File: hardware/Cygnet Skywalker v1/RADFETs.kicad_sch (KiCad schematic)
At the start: 18 parts, among them Q2 NJFET, Q3 NJFET, Q4 NMOS, Q5 NMOS, U11 RM-VT01-A Readout Module, U17 LM234Z-6, U6 VT01

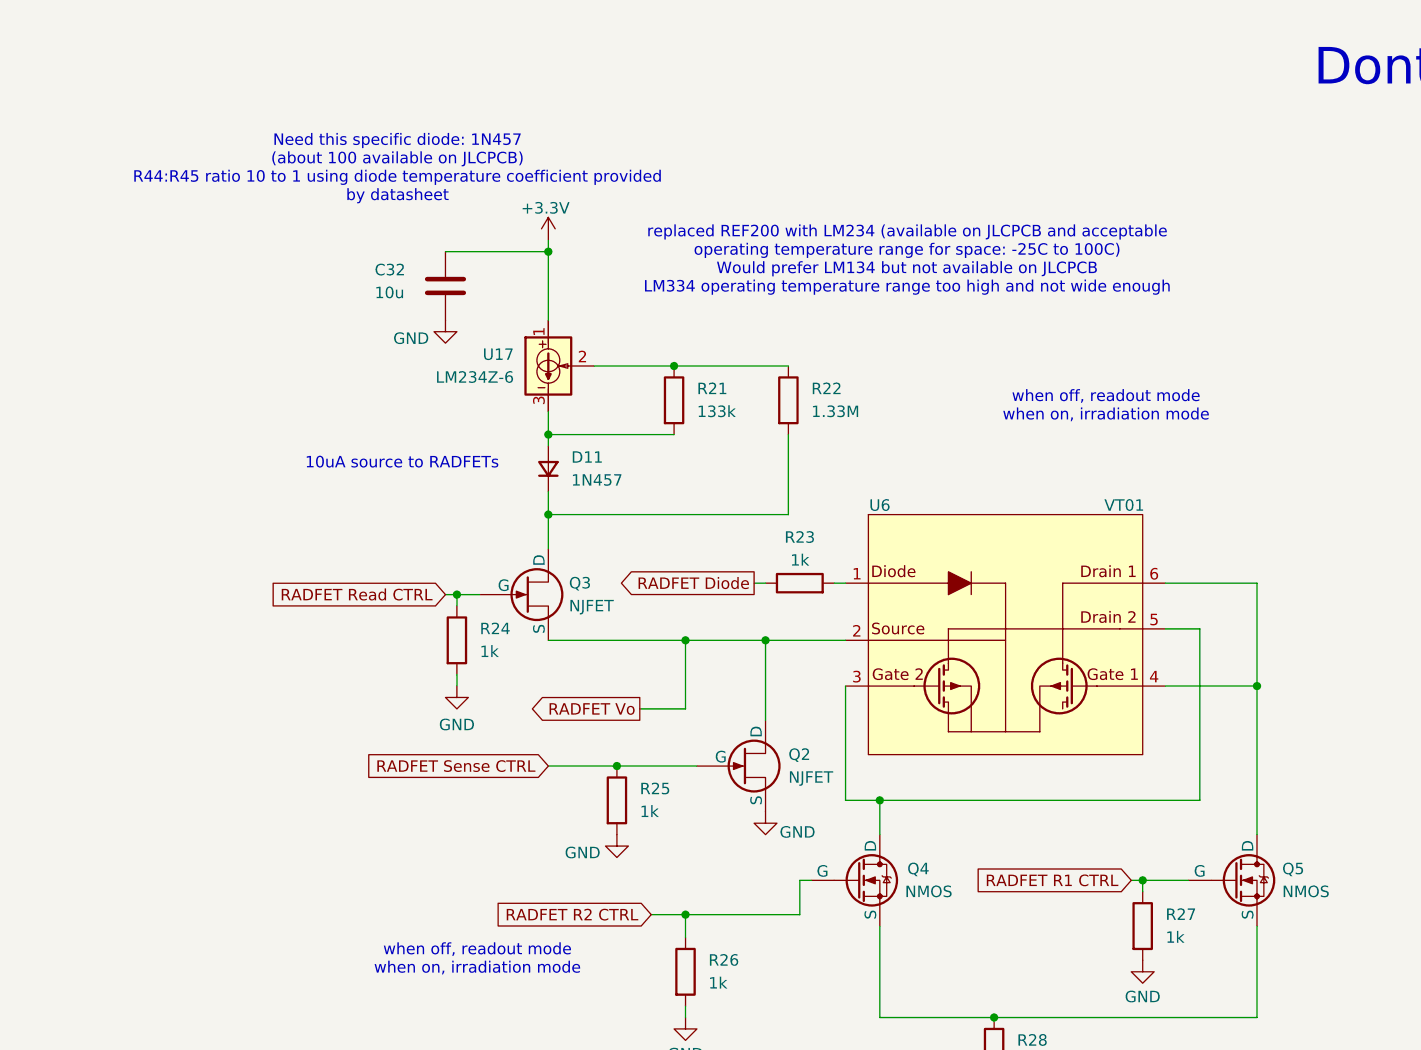
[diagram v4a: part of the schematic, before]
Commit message: updated schematic with mosfets
jfets no more for now. Also added footprints to some symbols.
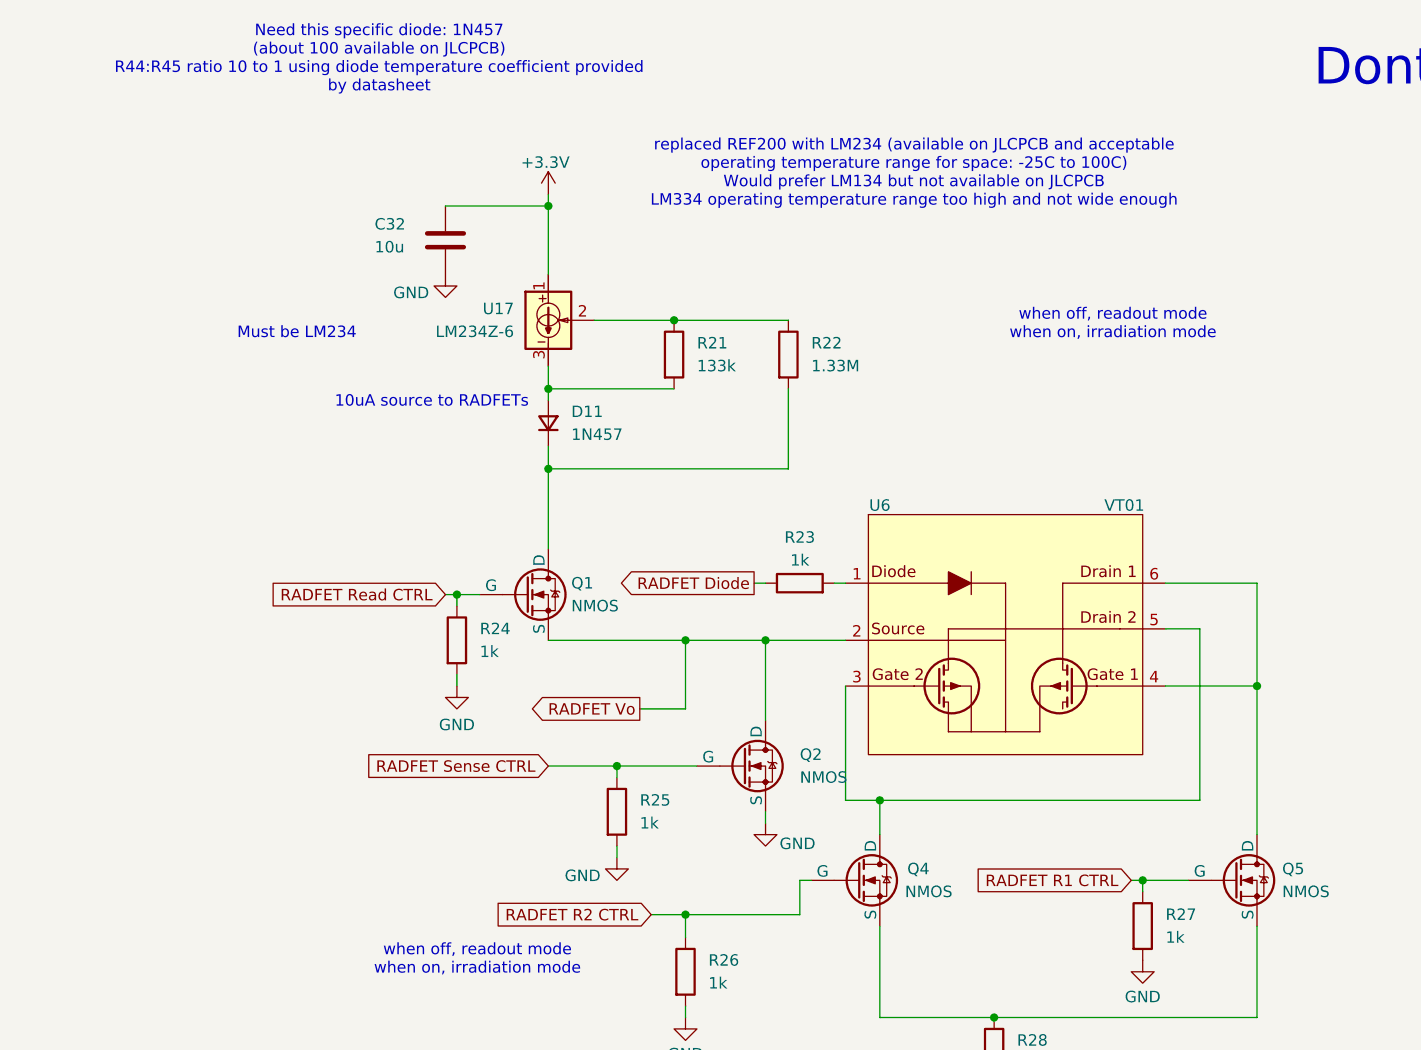
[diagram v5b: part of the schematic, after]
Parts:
- removed Q2, Q3: NJFET, symbol Simulation_SPICE:NJFET
- added Q1, Q2: NMOS, symbol Simulation_SPICE:NMOS
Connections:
- net GND: now also Q2.3 (S)
- net RADFET Read CTRL: now also Q1.2 (G)
- net RADFET Sense CTRL: now also Q2.2 (G)
- net RADFET Vo: now also Q1.3 (S), Q2.1 (D)
- net at D11.1 (K), R22.2: now also Q1.1 (D)
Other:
- note added: "Must be LM234"
- moved on the sheet: C32, D11, R21, R22, R25, U17

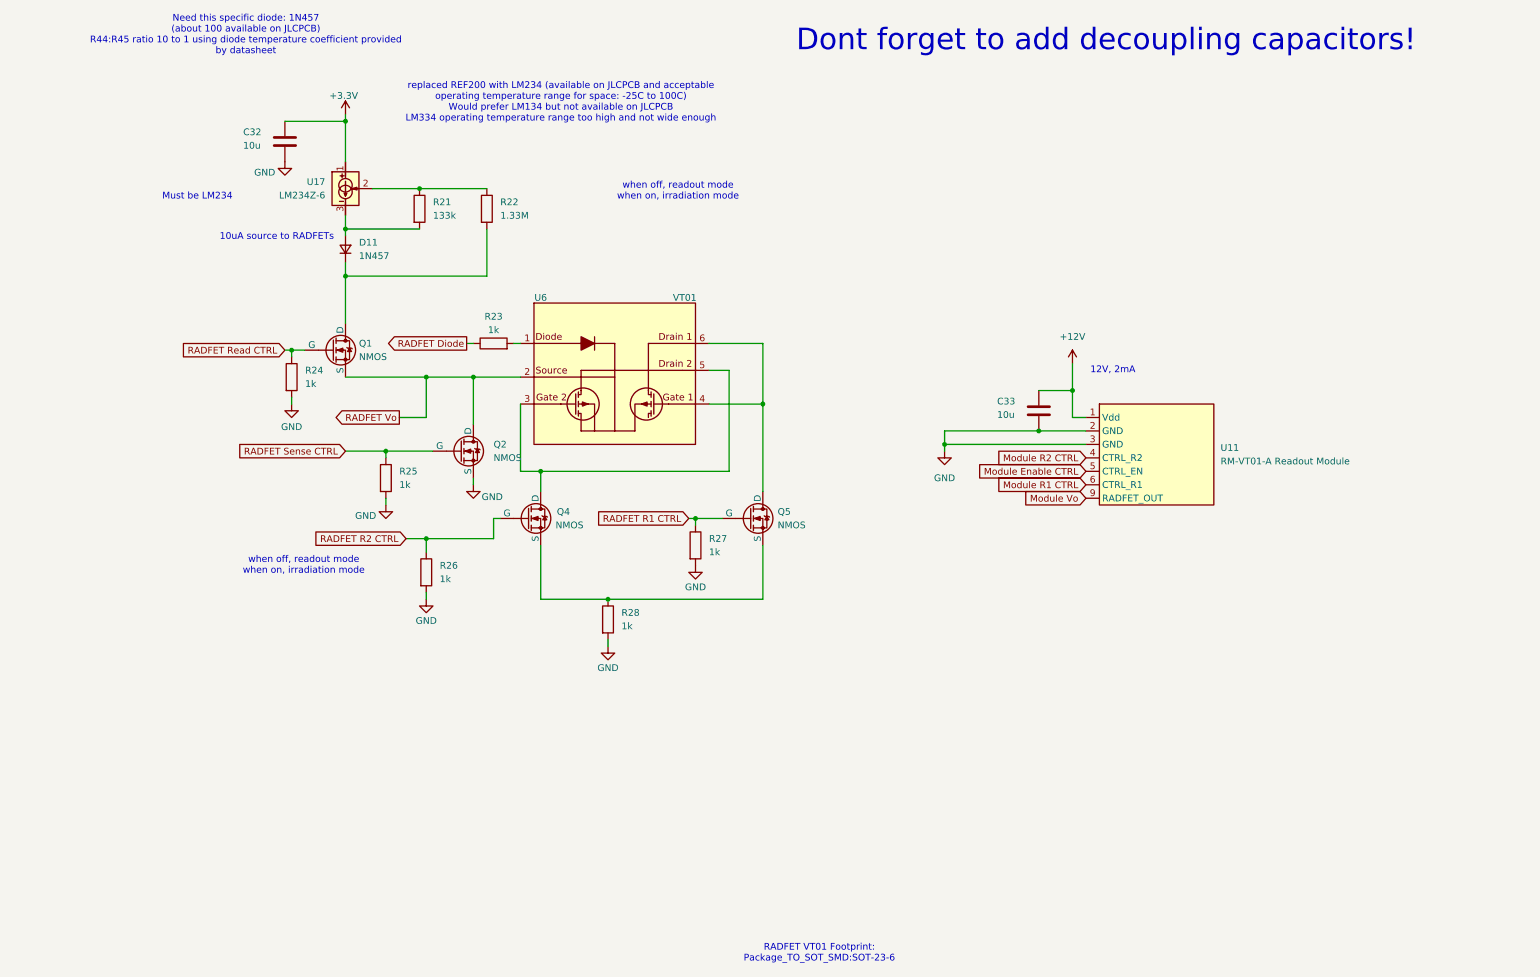
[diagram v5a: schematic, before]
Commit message: changes to radfet readout design
- using analog switch ic to switch between sense & readout (tmux1133)
- added non inverting buffer for voltage readout
- haven't fully deep dived into the new components & must look into more
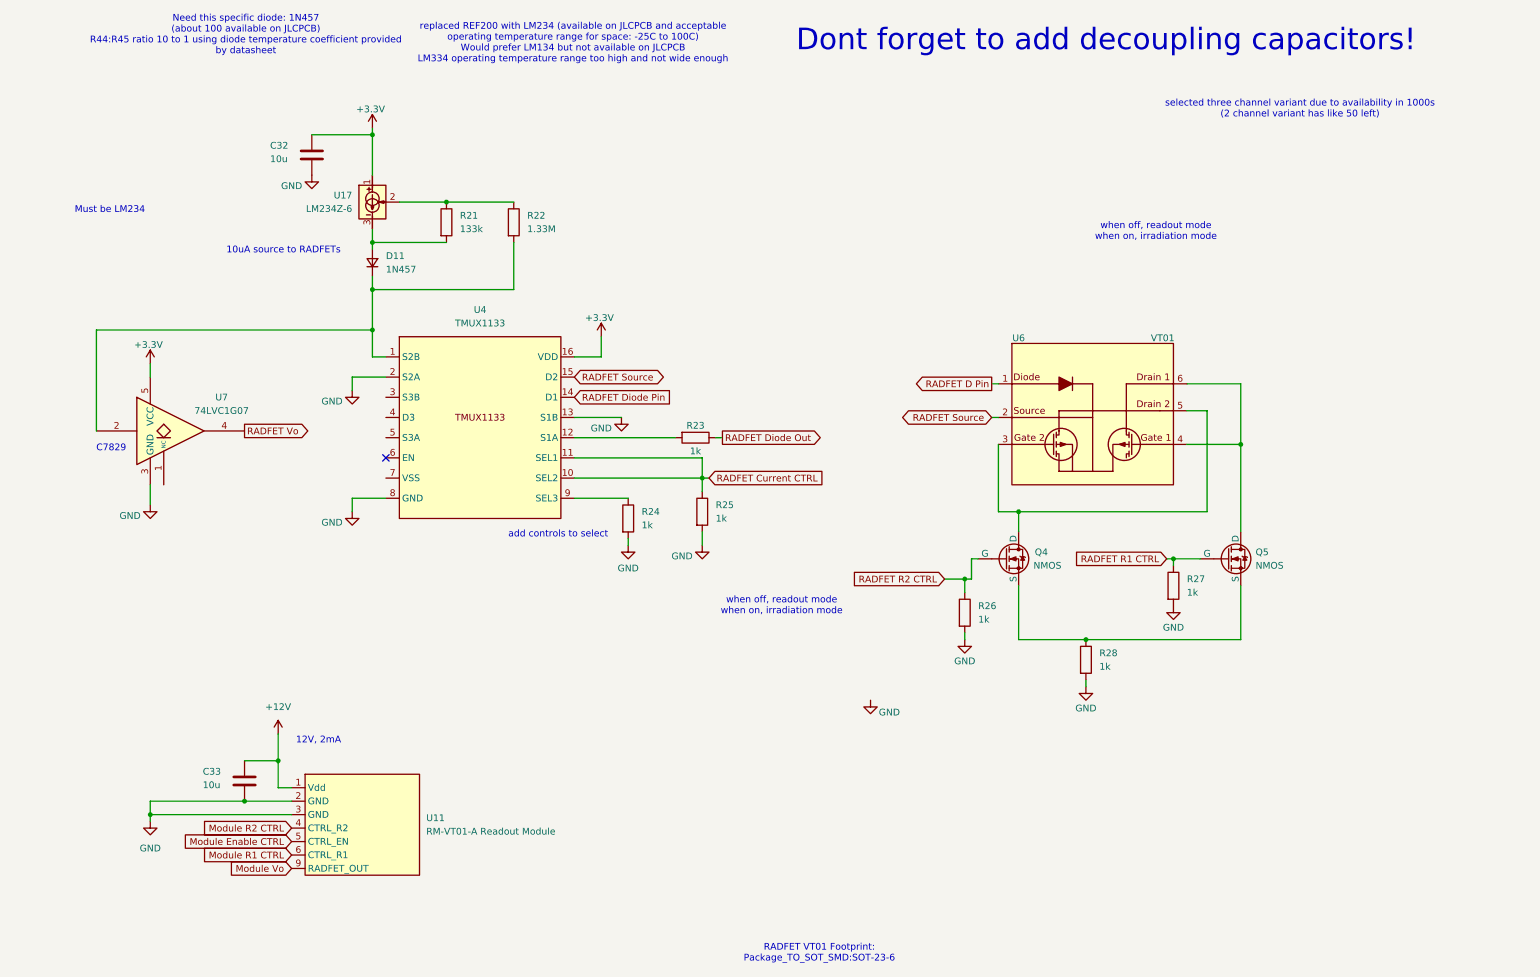
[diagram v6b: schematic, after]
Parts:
- removed Q1, Q2: NMOS, symbol Simulation_SPICE:NMOS
- added U4: TMUX1133, symbol Cygnet Skywalker v1:TMUX1133
- added U7: 74LVC1G07, Package_TO_SOT_SMD:SOT-23-5, symbol 74xGxx:74LVC1G07
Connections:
- net +3.3V: now also U4.16 (VDD), U7.5 (VCC)
- net GND: now also U4.13 (S1B), U4.2 (S2A), U4.8 (GND), U7.3 (GND)
- net RADFET Vo: now also U7.4; no longer U6.2
- net at R23.2: now also U4.12 (S1A); no longer U6.1
- net at D11.1 (K), R22.2: now also U4.1 (S2B), U7.2
- net RADFET Diode renamed RADFET Diode Out
- net RADFET Read CTRL: no longer names the net of R24.1
- net RADFET Read CTRL: now also U4.9 (SEL3)
- net RADFET Sense CTRL renamed RADFET Current CTRL
- net RADFET Current CTRL: now also U4.10 (SEL2), U4.11 (SEL1)
- new net RADFET D Pin: U6.1
- new net RADFET Diode Pin: U4.14 (D1)
- new net RADFET Source: U4.15 (D2), U6.2
- no-connect marks 0 -> 1
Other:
- note added: "C7829"
- note added: "add controls to select"
- note added: "selected three channel variant due to availability in 1000s (2 channel variant has like 50 left)"
- moved on the sheet: C32, C33, D11, Q4, Q5, R21, R22, R23, R24, R25, R26, R27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

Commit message: added op amp
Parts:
- added U15: OPA4H199-SEP, symbol Cygnet Skywalker v1:OPA4H199-SEP
- U4: footprint (none) -> Package_SO:TSSOP-16_4.4x5mm_P0.65mm
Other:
- note added: "OP AMP with +-10nA current leakage max"
- note added: "just found out leakage current is around +-5uA :skull:"
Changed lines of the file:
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@@
 	(generator_version "9.0")
 	(paper "A4")
+	(text "just found out leakage current is around +-5uA :skull:"
+		(exclude_from_sim no)
+		(at 38.354 106.426 0)
+		(effects
+			(font
+				(size 1.27 1.27)
+			)
+		)
+	)
 	(text "add controls to select"
 		(exclude_from_sim no)
@@
 		)
 	)
+	(text "OP AMP with +-10nA current leakage max"
+		(exclude_from_sim no)
+		(at 118.364 127.254 0)
+		(effects
+			(font
+				(size 1.27 1.27)
+			)
+		)
+	)
 	(text "Dont forget to add decoupling capacitors!"
 		(exclude_from_sim no)
@@
 	(text "when off, readout mode\nwhen on, irradiation mode"
 		(exclude_from_sim no)
-		(at 150.876 128.27 0)
+		(at 245.872 156.21 0)
 		(effects
 			(font
@@
 	)
 	(symbol
+		(lib_id "Cygnet Skywalker v1:OPA4H199-SEP")
+		(at 139.7 134.62 0)
+		(unit 1)
+		(exclude_from_sim no)
+		(in_bom yes)
+		(on_board yes)
+		(dnp no)
+		(fields_autoplaced yes)
+		(property "Reference" "U15"
+			(at 139.7 129.54 0)
+			(effects
+				(font
+					(size 1.27 1.27)
+				)
+			)
+		)
+		(property "Value" "OPA4H199-SEP"
+			(at 139.7 132.08 0)
+			(effects
+				(font
+					(size 1.27 1.27)
+				)
+			)
+		)
+		(property "Footprint" ""
+			(at 139.7 134.62 0)
+			(effects
+				(font
+					(size 1.27 1.27)
+				)
+				(hide yes)
+			)
+		)
+		(property "Datasheet" ""
+			(at 139.7 134.62 0)
+			(effects
+				(font
+					(size 1.27 1.27)
+				)
+				(hide yes)
+			)
+		)
+		(property "Description" ""
+			(at 139.7 134.62 0)
+			(effects
+				(font
+					(size 1.27 1.27)
+				)
+				(hide yes)
+			)
+		)
+		(pin "6"
+		)
+		(pin "8"
+		)
+		(pin "4"
+		)
+		(pin "5"
+		)
+		(pin "12"
+		)
+		(pin "2"
+		)
+		(pin "9"
+		)
+		(pin "1"
+		)
+		(pin "14"
+		)
+		(pin "3"
+		)
+		(pin "10"
+		)
+		(pin "13"
+		)
+		(pin "7"
+		)
+		(pin "11"
+		)
+		(instances
+			(project ""
+				(path "/f674abc6-f811-4b69-a04b-9059ca6b6a44/33e54b08-8438-48ba-af26-405155868428"
+					(reference "U15")
+					(unit 1)
+				)
+			)
+		)
+	)
+	(symbol
 		(lib_id "Device:R")
 		(at 208.28 138.43 0)
@@
 			)
 		)
-		(property "Footprint" ""
+		(property "Footprint" "Package_SO:TSSOP-16_4.4x5mm_P0.65mm"
 			(at 93.98 77.47 0)
 			(effects
@@
 					(unit 1)
 				)
-			)
-		)
-	)
-	(symbol
-		(lib_id "power:GND")
-		(at 167.64 146.05 0)
-		(unit 1)
-		(exclude_from_sim no)
-		(in_bom yes)
-		(on_board yes)
-		(dnp no)
-		(property "Reference" "#PWR050"
-			(at 167.64 152.4 0)
-			(effects
-				(font
-					(size 1.27 1.27)
-				)
-				(hide yes)
-			)
-		)
-		(property "Value" "GND"
-			(at 171.196 148.336 0)
-			(effects
-				(font
-					(size 1.27 1.27)
-				)
-			)
-		)
-		(property "Footprint" ""
-			(at 167.64 146.05 0)
-			(effects
-				(font
-					(size 1.27 1.27)
-				)
-				(hide yes)
-			)
-		)
-		(property "Datasheet" ""
-			(at 167.64 146.05 0)
-			(effects
-				(font
-					(size 1.27 1.27)
-				)
-				(hide yes)
-			)
-		)
-		(property "Description" "Power symbol creates a global label with name \"GND\" , ground"
-			(at 167.64 146.05 0)
-			(effects
-				(font
-					(size 1.27 1.27)
-				)
-				(hide yes)
-			)
-		)
-		(pin "1"
-		)
-		(instances
-			(project "Cygnet Skywalker v1"
-				(path "/f674abc6-f811-4b69-a04b-9059ca6b6a44/33e54b08-8438-48ba-af26-405155868428"
-					(reference "#PWR050")
-					(unit 1)
-				)
